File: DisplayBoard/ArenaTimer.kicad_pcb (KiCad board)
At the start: 2 copper layers, 262.2 x 230 mm, 213 parts, among them J1 Blue ready-up, J10 Red ready-up, J12 Screw_Terminal_01x03, J13 WAGO, J14 WAGO, J15 Conn_01x15_Socket, J16 Conn_01x15_Socket, J2 Conn_01x02_Socket, J3 Conn_01x02_Pin, J4 GND, J5 5V, J6 GND, J7 5V, J8 PJ-082BH, J9 Conn_01x06_Pin, K1 G5V-2_Split, Q1 BSS214NW

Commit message: clean up silk, resolve DRCs
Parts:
- J12: footprint TerminalBlock:TerminalBlock_bornier-3_P5.08mm -> TerminalBlock:TerminalBlock_MaiXu_MX126-5.0-03P_1x03_P5.00mm
- moved J12 0.27 mm to (56.1, 29.4)
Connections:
- J15 pad 5: unconnected-(J15-Pin_5-Pad5) -> RELAY_EN
- J3 pad 1: /TimerBorder/DOUT -> /TimerColon/DOUT
- J3 pad 2: /TimerColon/DOUT -> /TimerBorder/DOUT
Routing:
- net RELAY_EN: track 124.3 -> 131.3 mm, vias 1 -> 2
- net +3.3V: track 272.4 -> 271.3 mm
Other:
- board text added: "HW V3, 6/26"

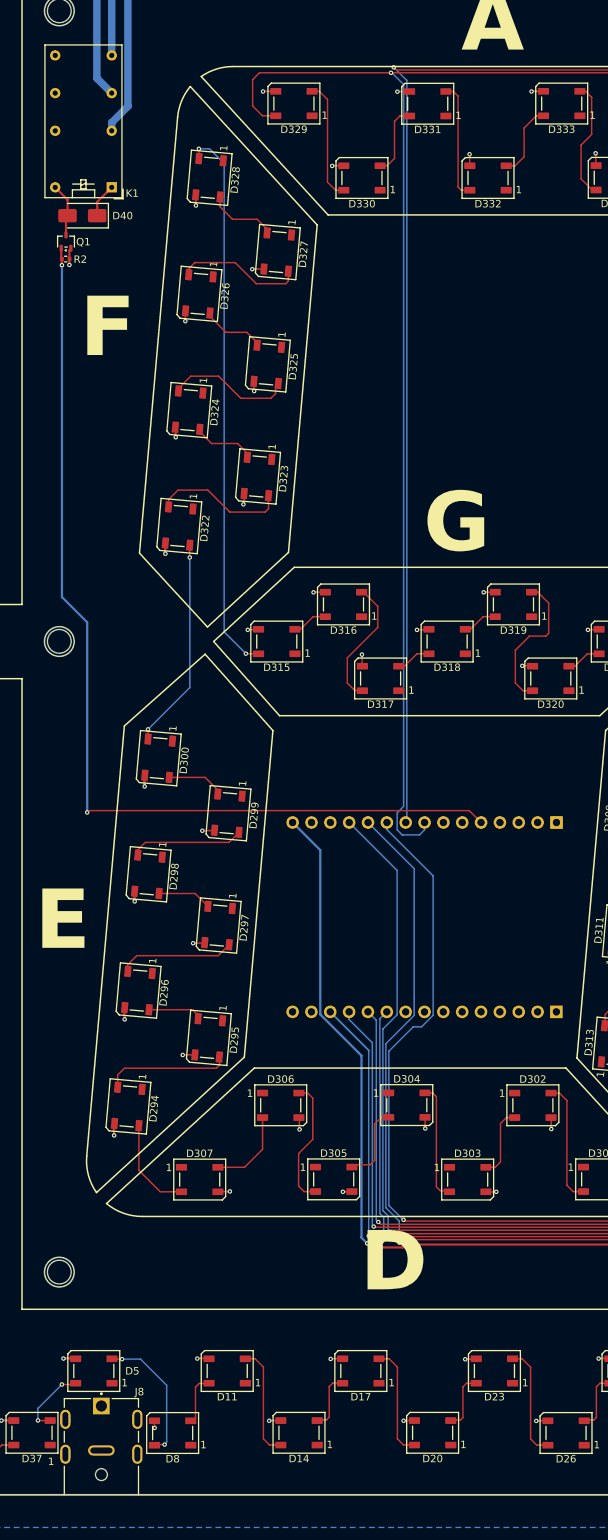
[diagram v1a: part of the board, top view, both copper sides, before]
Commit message: more cleanup, added spare IO and power pads for expansion
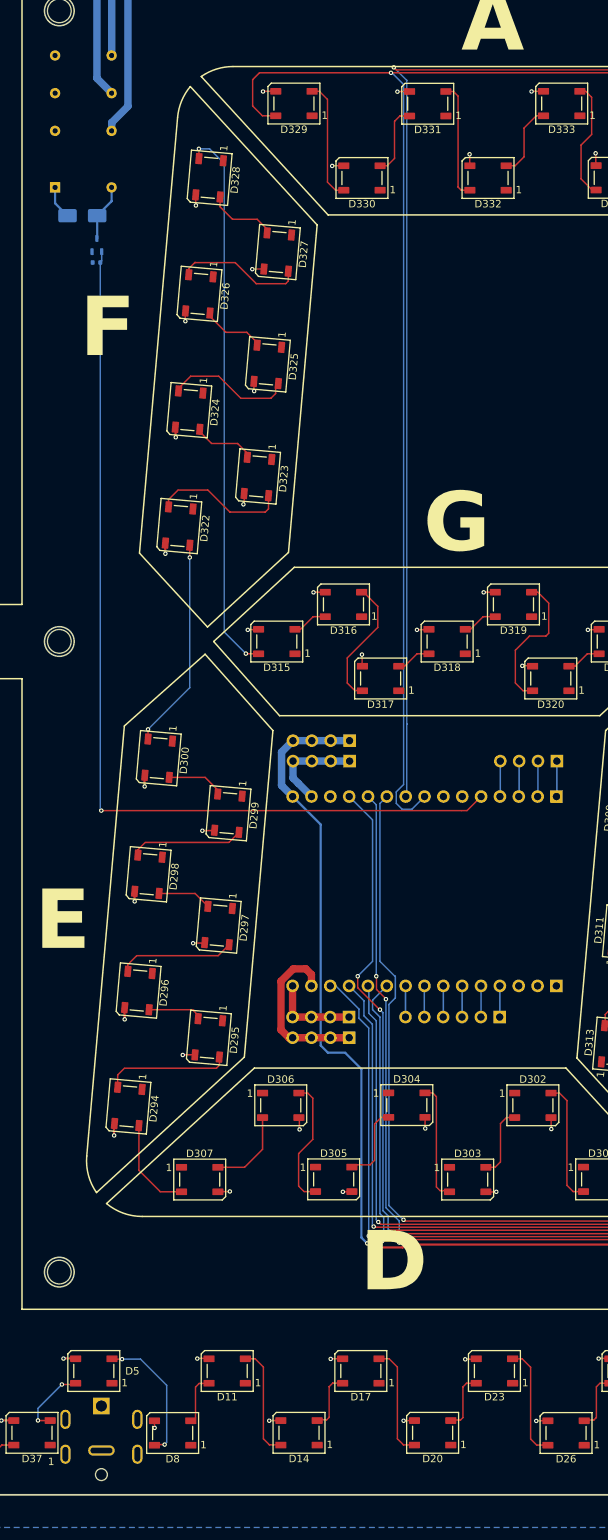
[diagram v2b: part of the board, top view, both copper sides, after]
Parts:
- added G***: LOGO, SEMO:SEMO, B.Cu at (181.9, 117.8)
- added J11: SPARE_IO, Connector_PinHeader_2.54mm:PinHeader_1x06_P2.54mm_Vertical, B.Cu at (115.1, 191.0)
- added J17: SPARE IO, Connector_PinHeader_2.54mm:PinHeader_1x04_P2.54mm_Vertical, B.Cu at (122.8, 156.5)
- added J18: SPARE 3.3V, Connector_PinHeader_2.54mm:PinHeader_1x04_P2.54mm_Vertical, B.Cu at (94.9, 153.7)
- added J19: SPARE 5V, Connector_PinHeader_2.54mm:PinHeader_1x04_P2.54mm_Vertical, B.Cu at (94.8, 191.0)
- added J20: SPARE GND, Connector_PinHeader_2.54mm:PinHeader_1x04_P2.54mm_Vertical, B.Cu at (94.8, 193.8)
- added J21: SPARE GND, Connector_PinHeader_2.54mm:PinHeader_1x04_P2.54mm_Vertical, B.Cu at (94.9, 156.5)
- D40, J8, K1, Q1, R2: moved to B.Cu
- moved K1 7.64 mm to (55.2, 79.2), turned to 0 degrees
- moved Q1 4.18 mm to (60.8, 86.9)
- moved R2 4.18 mm to (60.8, 89.3), turned to 180 degrees
- moved J15 3.50 mm to (122.8, 161.3)
- moved J16 3.50 mm to (122.8, 186.8)
- turned D40 to 0 degrees
- turned J8 to 180 degrees
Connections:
- J15 pad 1: unconnected-(J15-Pin_1-Pad1) -> Net-(J15-Pin_1)
- J15 pad 2: unconnected-(J15-Pin_2-Pad2) -> Net-(J15-Pin_2)
- J15 pad 3: unconnected-(J15-Pin_3-Pad3) -> Net-(J15-Pin_3)
- J15 pad 4: unconnected-(J15-Pin_4-Pad4) -> Net-(J15-Pin_4)
- J16 pad 4: unconnected-(J16-Pin_4-Pad4) -> Net-(J11-Pin_1)
- J16 pad 5: unconnected-(J16-Pin_5-Pad5) -> Net-(J11-Pin_2)
- J16 pad 6: unconnected-(J16-Pin_6-Pad6) -> Net-(J11-Pin_3)
- J16 pad 7: unconnected-(J16-Pin_7-Pad7) -> Net-(J11-Pin_4)
- J16 pad 8: unconnected-(J16-Pin_8-Pad8) -> Net-(J11-Pin_5)
- J16 pad 9: unconnected-(J16-Pin_9-Pad9) -> Net-(J11-Pin_6)
- K1 pad 11: (no net) -> Net-(J12-Pin_1)
- K1 pad 13: (no net) -> Net-(J12-Pin_3)
- K1 pad 4: Net-(J12-Pin_3) -> unconnected-(K1-Pad4)
- K1 pad 6: Net-(J12-Pin_1) -> unconnected-(K1-Pad6)
- K1 pad 8: Net-(J12-Pin_2) -> unconnected-(K1-Pad8)
- K1 pad 9: (no net) -> Net-(J12-Pin_2)
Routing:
- net GND: track 292.2 -> 326.3 mm, vias 179 -> 178
- net +3.3V: track 271.3 -> 292.5 mm
- net +5V: track 4.63 -> 16.3 mm
- net Net-(J15-Pin_3): track 0.00 -> 5.11 mm
- net Net-(J15-Pin_2): track 0.00 -> 5.11 mm
- net Net-(J15-Pin_4): track 0.00 -> 5.11 mm
- net Net-(J15-Pin_1): track 0.00 -> 5.11 mm
- net nSTART_BTN: track 215.6 -> 219.9 mm
- net Net-(J11-Pin_3): track 0.00 -> 4.23 mm
- net Net-(J11-Pin_1): track 0.00 -> 4.23 mm
- net Net-(J11-Pin_4): track 0.00 -> 4.23 mm
- net Net-(J11-Pin_2): track 0.00 -> 4.23 mm
- net Net-(J11-Pin_5): track 0.00 -> 4.21 mm
- net Net-(J11-Pin_6): track 0.00 -> 4.21 mm
- net DIGIT_LEDS: track 321.4 -> 317.5 mm
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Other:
- board text added: "+3.3V GND"
- board text added: "+5V GND"
- board text added: "D23 D22 TX0 RX0"
- board text added: "D34 D35 D32 D33 D25 D26"
- board text added: "Do not exceed 2A load!"
- board text added: "ESP32, Power Jack, Relay, and screw terminal only need to be popluated one one board per timer!"
- board text added: "Minimum Input Requirements: Single sided: 5V, 10A = 50W adapter Double sided: 5V, 15A = 75W adapter"
- board text removed: "+5V Input Only!"
- board text removed: "ESP32, Power Jack, Relay, and screw terminals only need to be popluated one one board per timer!"

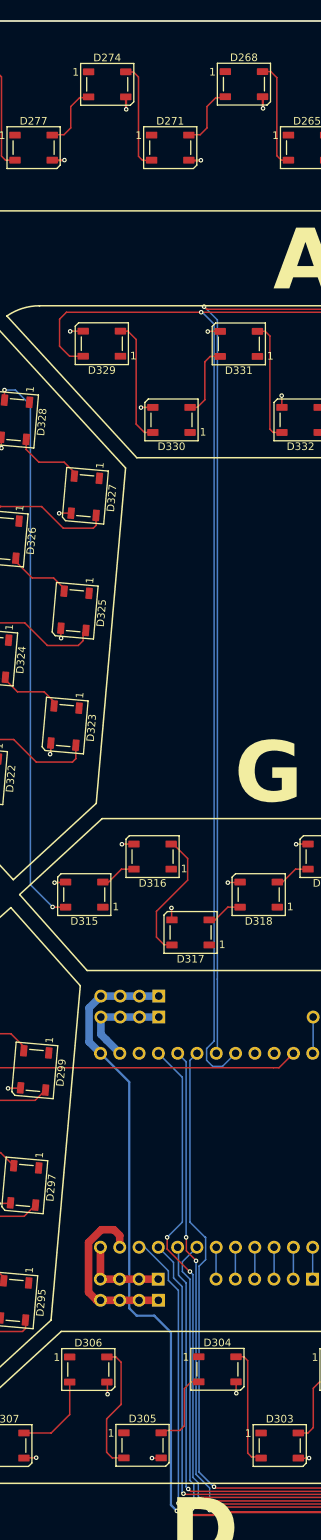
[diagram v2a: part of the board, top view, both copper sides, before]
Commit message: add beeper, generate production files
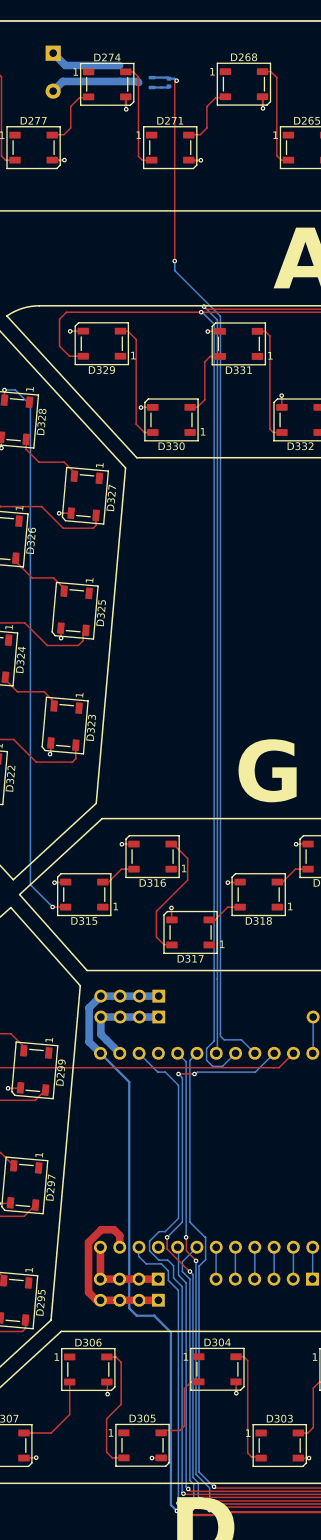
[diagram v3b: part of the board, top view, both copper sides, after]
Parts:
- added BZ1: CEM-1203(42), Buzzer_Beeper:Buzzer_TDK_PS1240P02BT_D12.2mm_H6.5mm, B.Cu at (81.0, 29.6)
- added D41: 1N4148WS, SOD323, Diode_SMD:D_SOD-323, B.Cu at (89.8, 32.3)
- added Q2: BSS138, Package_TO_SOT_SMD:SOT-323_SC-70, B.Cu at (93.1, 33.5)
- added R10: 100K, Resistor_SMD:R_0402_1005Metric, B.Cu at (96.2, 33.5)
- Q1: value BSS214NW -> BSS138
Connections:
- J15 pad 12: nBUZZER_BTN -> unconnected-(J15-Pin_12-Pad12)
- J15 pad 13: unconnected-(J15-Pin_13-Pad13) -> nRESET_BTN
- J15 pad 6: unconnected-(J15-Pin_6-Pad6) -> nBUZZER_BTN
- J15 pad 7: unconnected-(J15-Pin_7-Pad7) -> BEEPER_EN
- J16 pad 12: nRESET_BTN -> unconnected-(J16-Pin_12-Pad12)
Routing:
- net BEEPER_EN: track 0.00 -> 137.2 mm, vias 0 -> 2
- net nRESET_BTN: track 223.6 -> 255.1 mm
- net Net-(BZ1--): track 0.00 -> 11.8 mm
- net nBUZZER_BTN: track 252.0 -> 261.9 mm, vias 4 -> 6
- net +5V: track 16.3 -> 25.8 mm
- net GND: track 326.3 -> 328.5 mm
- net nTIME_SEL: track 226.6 -> 227.3 mm
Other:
- board text added: "V3 6/26"
- board text removed: "HW V3, 6/26"
